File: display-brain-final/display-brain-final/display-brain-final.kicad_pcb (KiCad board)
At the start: 2 copper layers, 104.2 x 68 mm, 24 parts, among them J1 Conn_01x02_Socket, J2 Conn_01x05_Socket, J3 Conn_01x19_Socket, J4 Conn_01x19_Socket, J5 Conn_01x04_Socket, J6 Conn_01x05_Socket, J7 Conn_01x02_Socket, P1 USB_C_Plug_USB2.0, U3 LM317_TO-252

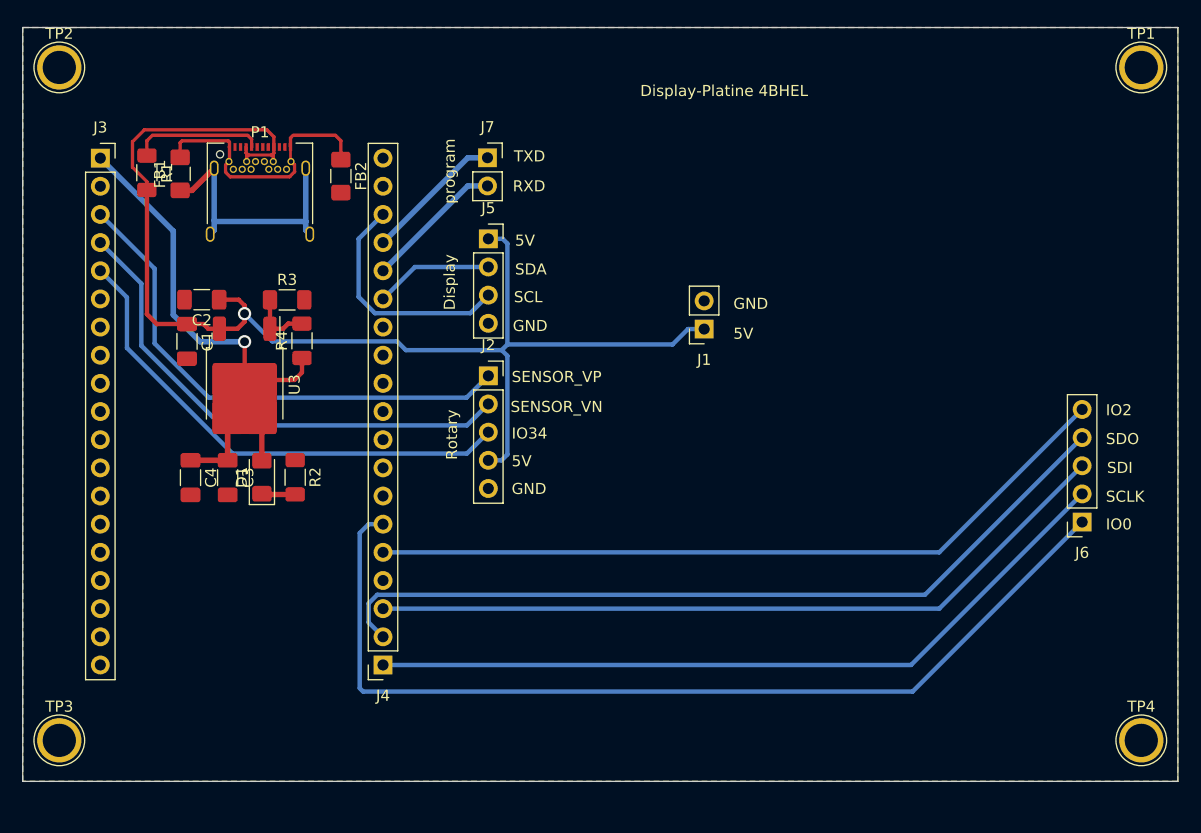
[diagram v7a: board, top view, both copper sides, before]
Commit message: display and funk changed
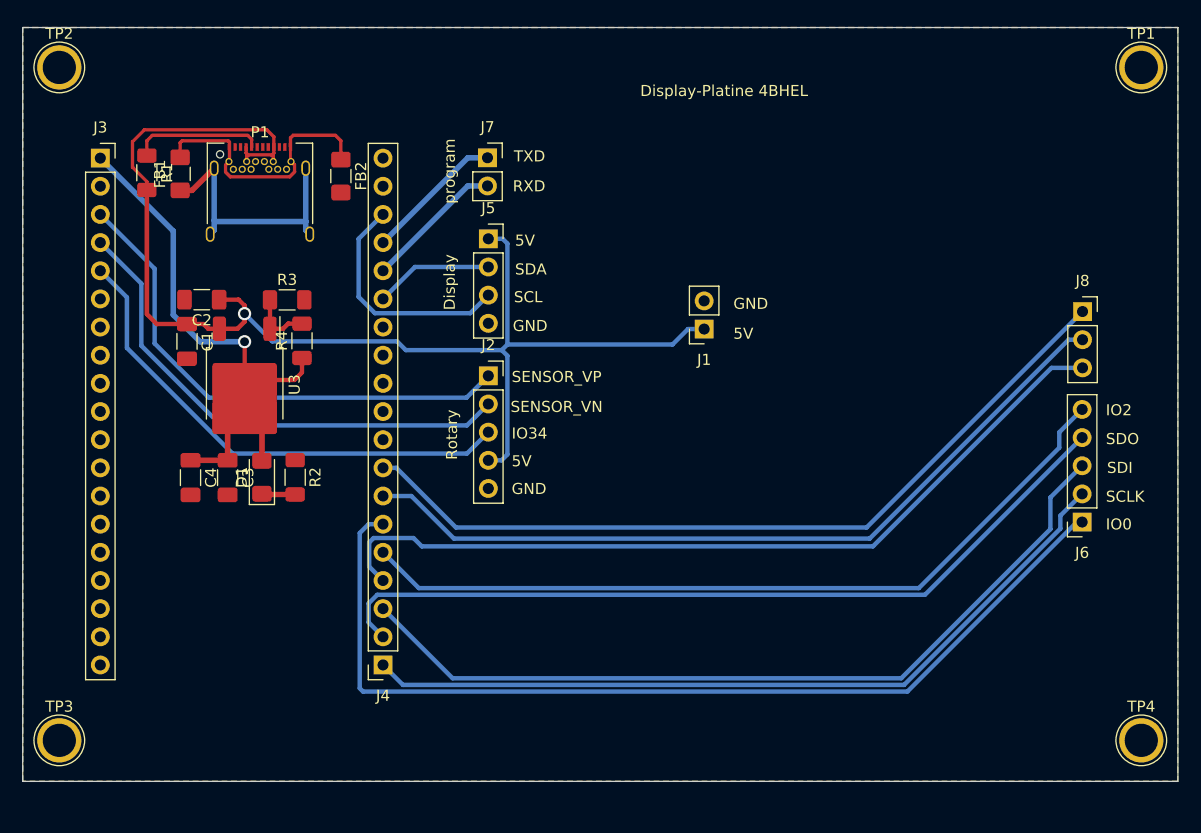
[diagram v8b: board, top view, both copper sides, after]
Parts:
- added J8: Conn_01x03_Socket, Connector_PinSocket_2.54mm:PinSocket_1x03_P2.54mm_Vertical, F.Cu at (221.7, 74.3)
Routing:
- net /IO15: track 0.00 -> 75.4 mm
- net /IO16: track 0.00 -> 73.4 mm
- net /IO4: track 0.00 -> 72.1 mm
- net /SD1: track 68.4 -> 75.3 mm
- net /IO2: track 68.4 -> 72.4 mm
- net /CLK: track 69.5 -> 71.6 mm
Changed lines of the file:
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@@
+    )
+  )
+  (footprint "Connector_PinSocket_2.54mm:PinSocket_1x03_P2.54mm_Vertical" (layer "F.Cu")
+    (at 221.7 74.32)
+    (descr "Through hole straight socket strip, 1x03, 2.54mm pitch, single row (from Kicad 4.0.7), script generated")
+    (tags "Through hole socket strip THT 1x03 2.54mm single row")
+    (property "Sheetfile" "display-brain-final.kicad_sch")
+    (property "Sheetname" "")
+    (property "ki_description" "Generic connector, single row, 01x03, script generated")
+    (property "ki_keywords" "connector")
+    (attr through_hole)
+    (fp_text reference "J8" (at 0 -2.77) (layer "F.SilkS")
+        (effects (font (size 1 1) (thickness 0.15)))
+    )
+    (fp_text value "Conn_01x03_Socket" (at 0 7.85) (layer "F.Fab")
+        (effects (font (size 1 1) (thickness 0.15)))
+    )
+    (fp_text user "${REFERENCE}" (at 0 2.54 90) (layer "F.Fab")
+        (effects (font (size 1 1) (thickness 0.15)))
+    )
+    (fp_line (start -1.33 1.27) (end -1.33 6.41)
+      (stroke (width 0.12) (type solid)) (layer "F.SilkS"))
+    (fp_line (start -1.33 1.27) (end 1.33 1.27)
+      (stroke (width 0.12) (type solid)) (layer "F.SilkS"))
+    (fp_line (start -1.33 6.41) (end 1.33 6.41)
+      (stroke (width 0.12) (type solid)) (layer "F.SilkS"))
+    (fp_line (start 0 -1.33) (end 1.33 -1.33)
+      (stroke (width 0.12) (type solid)) (layer "F.SilkS"))
+    (fp_line (start 1.33 -1.33) (end 1.33 0)
+      (stroke (width 0.12) (type solid)) (layer "F.SilkS"))
+    (fp_line (start 1.33 1.27) (end 1.33 6.41)
+      (stroke (width 0.12) (type solid)) (layer "F.SilkS"))
+    (fp_line (start -1.8 -1.8) (end 1.75 -1.8)
+      (stroke (width 0.05) (type solid)) (layer "F.CrtYd"))
+    (fp_line (start -1.8 6.85) (end -1.8 -1.8)
+      (stroke (width 0.05) (type solid)) (layer "F.CrtYd"))
+    (fp_line (start 1.75 -1.8) (end 1.75 6.85)
+      (stroke (width 0.05) (type solid)) (layer "F.CrtYd"))
+    (fp_line (start 1.75 6.85) (end -1.8 6.85)
+      (stroke (width 0.05) (type solid)) (layer "F.CrtYd"))
+    (fp_line (start -1.27 -1.27) (end 0.635 -1.27)
+      (stroke (width 0.1) (type solid)) (layer "F.Fab"))
+    (fp_line (start -1.27 6.35) (end -1.27 -1.27)
+      (stroke (width 0.1) (type solid)) (layer "F.Fab"))
+    (fp_line (start 0.635 -1.27) (end 1.27 -0.635)
+      (stroke (width 0.1) (type solid)) (layer "F.Fab"))
+    (fp_line (start 1.27 -0.635) (end 1.27 6.35)
+      (stroke (width 0.1) (type solid)) (layer "F.Fab"))
+    (fp_line (start 1.27 6.35) (end -1.27 6.35)
+      (stroke (width 0.1) (type solid)) (layer "F.Fab"))
+    (pad "1" thru_hole rect (at 0 0) (size 1.7 1.7) (drill 1) (layers "*.Cu" "*.Mask")
+      (net 29 "/IO16") (pinfunction "Pin_1") (pintype "passive"))
+    (pad "2" thru_hole oval (at 0 2.54) (size 1.7 1.7) (drill 1) (layers "*.Cu" "*.Mask")
+      (net 28 "/IO4") (pinfunction "Pin_2") (pintype "passive"))
+    (pad "3" thru_hole oval (at 0 5.08) (size 1.7 1.7) (drill 1) (layers "*.Cu" "*.Mask")
+      (net 25 "/IO15") (pinfunction "Pin_3") (pintype "passive"))
+    (model "${KICAD6_3DMODEL_DIR}/Connector_PinSocket_2.54mm.3dshapes/PinSocket_1x03_P2.54mm_Vertical.wrl"
+      (offset (xyz 0 0 0))
+      (scale (xyz 1 1 1))
+      (rotate (xyz 0 0 0))
     )
   )
@@
   (segment (start 133.1 60.48) (end 139.68 67.06) (width 0.5) (layer "B.Cu") (net 8))
   (segment (start 139.68 74.62) (end 142.1 77.04) (width 0.5) (layer "B.Cu") (net 8))
-  (segment (start 206.234336 106.2) (end 221.664578 90.769758) (width 0.4) (layer "B.Cu") (net 22))
-  (segment (start 158.6 106.2) (end 206.234336 106.2) (width 0.4) (layer "B.Cu") (net 22))
+  (segment (start 205.6 108) (end 219.7 93.9) (width 0.4) (layer "B.Cu") (net 22))
+  (segment (start 160.4 108) (end 205.6 108) (width 0.4) (layer "B.Cu") (net 22))
+  (segment (start 219.7 92.734336) (end 221.664578 90.769758) (width 0.4) (layer "B.Cu") (net 22))
+  (segment (start 219.7 93.9) (end 219.7 92.734336) (width 0.4) (layer "B.Cu") (net 22))
+  (segment (start 158.6 106.2) (end 160.4 108) (width 0.4) (layer "B.Cu") (net 22))
   (segment (start 207.484336 99.87) (end 158.082233 99.87) (width 0.4) (layer "B.Cu") (net 23))
   (segment (start 221.664578 85.689758) (end 207.484336 99.87) (width 0.4) (layer "B.Cu") (net 23))
@@
   (segment (start 157.3 102.36) (end 158.6 103.66) (width 0.4) (layer "B.Cu") (net 23))
   (segment (start 157.3 100.652233) (end 157.3 102.36) (width 0.4) (layer "B.Cu") (net 23))
-  (segment (start 221.664578 88.229758) (end 208.774336 101.12) (width 0.4) (layer "B.Cu") (net 24))
-  (segment (start 208.774336 101.12) (end 158.6 101.12) (width 0.4) (layer "B.Cu") (net 24))
-  (segment (start 208.774336 96.04) (end 158.6 96.04) (width 0.4) (layer "B.Cu") (net 26))
-  (segment (start 221.664578 83.149758) (end 208.774336 96.04) (width 0.4) (layer "B.Cu") (net 26))
-  (segment (start 206.374336 108.6) (end 156.8 108.6) (width 0.4) (layer "B.Cu") (net 27))
-  (segment (start 221.664578 93.309758) (end 206.374336 108.6) (width 0.4) (layer "B.Cu") (net 27))
+  (segment (start 218.8 93.951472) (end 218.8 91.094336) (width 0.4) (layer "B.Cu") (net 24))
+  (segment (start 218.8 91.094336) (end 221.664578 88.229758) (width 0.4) (layer "B.Cu") (net 24))
+  (segment (start 164.88 107.4) (end 205.351472 107.4) (width 0.4) (layer "B.Cu") (net 24))
+  (segment (start 158.6 101.12) (end 164.88 107.4) (width 0.4) (layer "B.Cu") (net 24))
+  (segment (start 205.351472 107.4) (end 218.8 93.951472) (width 0.4) (layer "B.Cu") (net 24))
+  (segment (start 161.35 94.75) (end 157.75 94.75) (width 0.4) (layer "B.Cu") (net 25))
+  (segment (start 162.1 95.5) (end 161.35 94.75) (width 0.4) (layer "B.Cu") (net 25))
+  (segment (start 157.35 97.33) (end 158.6 98.58) (width 0.4) (layer "B.Cu") (net 25))
+  (segment (start 221.7 79.4) (end 218.9 79.4) (width 0.4) (layer "B.Cu") (net 25))
+  (segment (start 157.35 95.15) (end 157.35 97.33) (width 0.4) (layer "B.Cu") (net 25))
+  (segment (start 218.9 79.4) (end 202.8 95.5) (width 0.4) (layer "B.Cu") (net 25))
+  (segment (start 202.8 95.5) (end 162.1 95.5) (width 0.4) (layer "B.Cu") (net 25))
+  (segment (start 157.75 94.75) (end 157.35 95.15) (width 0.4) (layer "B.Cu") (net 25))
+  (segment (start 219.6 86.6) (end 206.93 99.27) (width 0.4) (layer "B.Cu") (net 26))
+  (segment (start 221.664578 83.149758) (end 221.150242 83.149758) (width 0.4) (layer "B.Cu") (net 26))
+  (segment (start 221.664578 83.149758) (end 219.6 85.214336) (width 0.4) (layer "B.Cu") (net 26))
+  (segment (start 219.6 85.214336) (end 219.6 86.6) (width 0.4) (layer "B.Cu") (net 26))
+  (segment (start 206.93 99.27) (end 161.83 99.27) (width 0.4) (layer "B.Cu") (net 26))
+  (segment (start 161.83 99.27) (end 158.6 96.04) (width 0.4) (layer "B.Cu") (net 26))
+  (segment (start 156.5 94.3) (end 157.3 93.5) (width 0.4) (layer "B.Cu") (net 27))
+  (segment (start 221.664578 93.309758) (end 221.190242 93.309758) (width 0.4) (layer "B.Cu") (net 27))
+  (segment (start 156.5 108.3) (end 156.5 94.3) (width 0.4) (layer "B.Cu") (net 27))
+  (segment (start 205.9 108.6) (end 156.8 108.6) (width 0.4) (layer "B.Cu") (net 27))
   (segment (start 157.3 93.5) (end 158.6 93.5) (width 0.4) (layer "B.Cu") (net 27))
-  (segment (start 156.5 108.3) (end 156.5 94.3) (width 0.4) (layer "B.Cu") (net 27))
-  (segment (start 156.5 94.3) (end 157.3 93.5) (width 0.4) (layer "B.Cu") (net 27))
+  (segment (start 221.190242 93.309758) (end 205.9 108.6) (width 0.4) (layer "B.Cu") (net 27))
   (segment (start 156.8 108.6) (end 156.5 108.3) (width 0.4) (layer "B.Cu") (net 27))
+  (segment (start 161.16 90.96) (end 158.6 90.96) (width 0.4) (layer "B.Cu") (net 28))
+  (segment (start 220.44 76.86) (end 202.5 94.8) (width 0.4) (layer "B.Cu") (net 28))
+  (segment (start 165 94.8) (end 161.16 90.96) (width 0.4) (layer "B.Cu") (net 28))
+  (segment (start 202.5 94.8) (end 165 94.8) (width 0.4) (layer "B.Cu") (net 28))
+  (segment (start 221.7 76.86) (end 220.44 76.86) (width 0.4) (layer "B.Cu") (net 28))
+  (segment (start 221.7 74.32) (end 202.22 93.8) (width 0.4) (layer "B.Cu") (net 29))
+  (segment (start 165.182081 93.8) (end 159.802081 88.42) (width 0.4) (layer "B.Cu") (net 29))
+  (segment (start 202.22 93.8) (end 165.182081 93.8) (width 0.4) (layer "B.Cu") (net 29))
+  (segment (start 159.802081 88.42) (end 158.6 88.42) (width 0.4) (layer "B.Cu") (net 29))
   (segment (start 161.48 70.3) (end 158.6 73.18) (width 0.4) (layer "B.Cu") (net 34))
   (segment (start 168.1 70.3) (end 161.48 70.3) (width 0.4) (layer "B.Cu") (net 34))
